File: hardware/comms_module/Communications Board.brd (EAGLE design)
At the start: 30 x 25 mm, 44 parts, among them U2 STC3115, X2 USB-MICROB

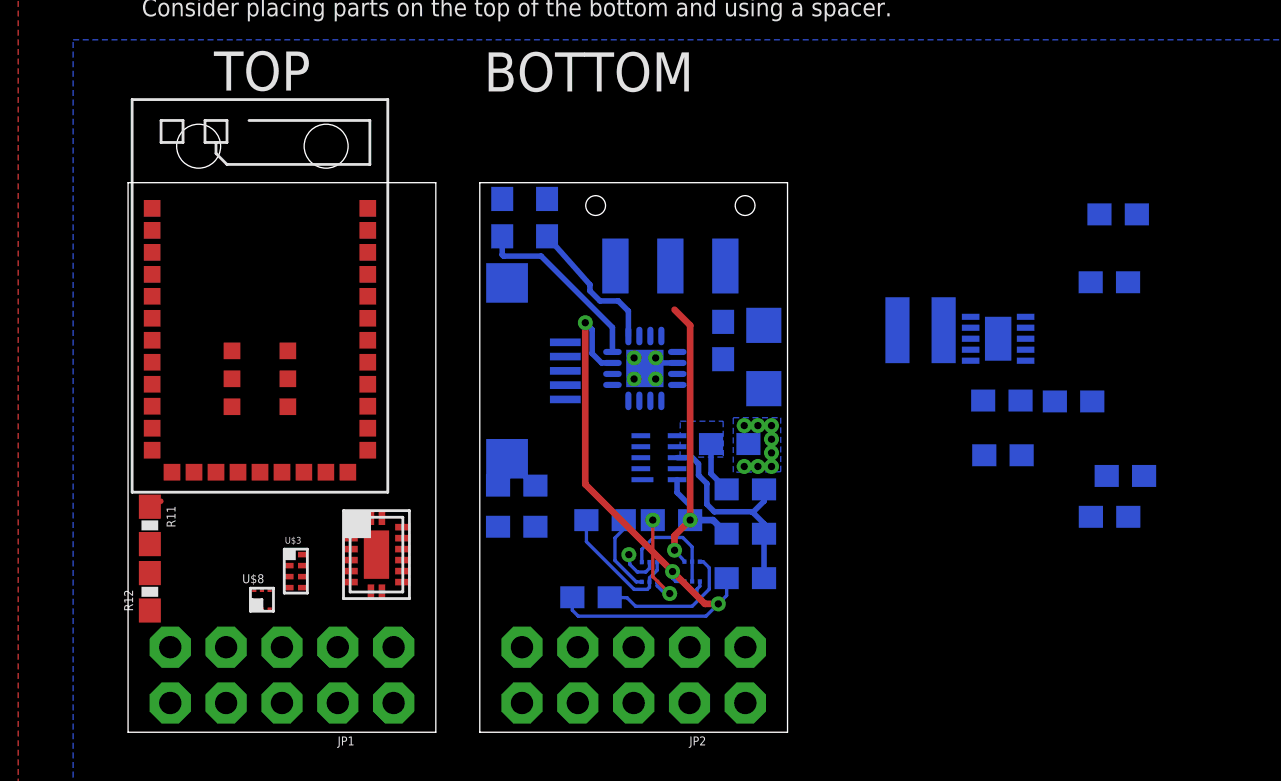
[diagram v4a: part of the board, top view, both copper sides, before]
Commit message: Continued routing of the communications board.
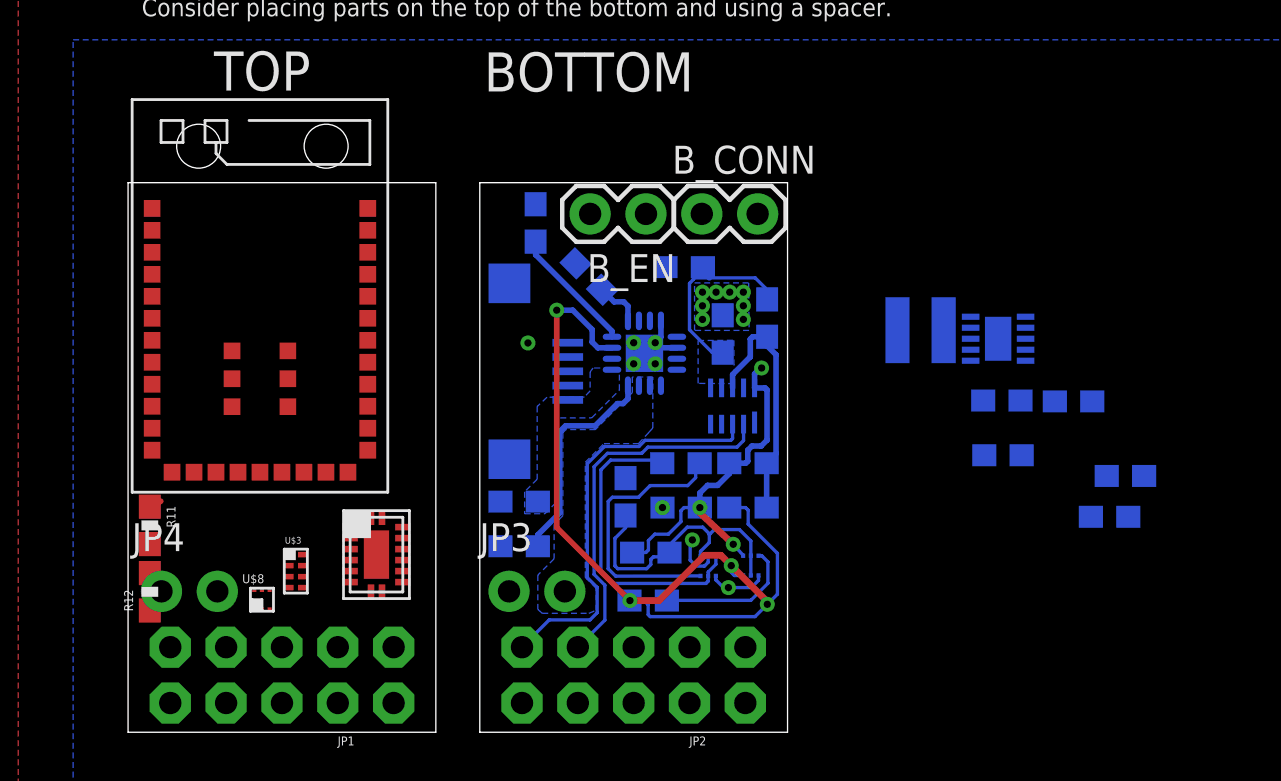
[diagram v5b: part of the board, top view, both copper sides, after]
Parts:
- removed PSW: (no value), Capstone Library:JS102011SAQN
- removed TP1, TP2: PTR1TP16SQ, testpad:TP16SQ
- added B_CONN, B_EN: (no value), SparkFun-Connectors:1X02
- added JP3, JP4: (no value), SparkFun-Connectors:1X02_NO_SILK
- moved R19 25.8 mm to (22.6, 10.7), turned to 270 degrees
- moved R18 24.2 mm to (23.8, 8.17), turned to 180 degrees
- moved R4 7.85 mm to (29.1, 18.8), turned to 270 degrees
- moved R5 5.02 mm to (27.1, 18.1), turned to 90 degrees
- moved R13 4.31 mm to (25.1, 12.2)
- moved U2 4.09 mm to (27.5, 14.8), turned to 0 degrees
- moved C5 3.78 mm to (25.3, 21.2), turned to 180 degrees
- moved R8 3.29 mm to (21.0, 20.7), turned to 225 degrees
- moved R17 3.21 mm to (28.2, 12.2)
- moved R6 3.21 mm to (28.2, 10.2)
- moved U$6 2.68 mm to (26.4, 7.56)
- moved U$7 2.68 mm to (28.3, 7.58)
- moved R16 2.60 mm to (23.7, 5.99)
- moved R7 1.54 mm to (18.5, 23.2)
- moved R2 0.90 mm to (17.8, 8.46)
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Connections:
- removed net N$6: PSW.3, TP2.TP
- new net B+IN: B_CONN.1, B_EN.1
- net +3V3: now also JP3.1, JP4.1
- net BAT+: now also B_EN.2; no longer PSW.2
- net BAT-: now also B_CONN.2; no longer TP1.TP
- net V_PREBUCK: now also JP3.2, JP4.2
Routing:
- net SCL: track 0.56 -> 19.3 mm
- net SDA: track 0.00 -> 17.0 mm
- net SYSOFF: track 28.1 -> 40.2 mm, vias 3 -> 4
- net N$23: track 0.00 -> 9.95 mm
- net N$12: track 3.63 -> 12.6 mm
- net N$22: track 4.84 -> 13.4 mm
- net N$9: track 6.08 -> 14.4 mm
- net BAT-: track 2.35 -> 8.97 mm
- net N$20: track 6.49 -> 2.16 mm
- net N$24: track 8.34 -> 5.77 mm
- net BATDC: track 9.79 -> 11.5 mm
- net GND: track 6.38 -> 5.49 mm, vias 14 -> 15
- net BAT+: track 16.2 -> 16.7 mm, vias 2 -> 3
- added copper zone on layer 16, net JACK_PWR
- added copper zone on layer 16, net V_PREBUCK

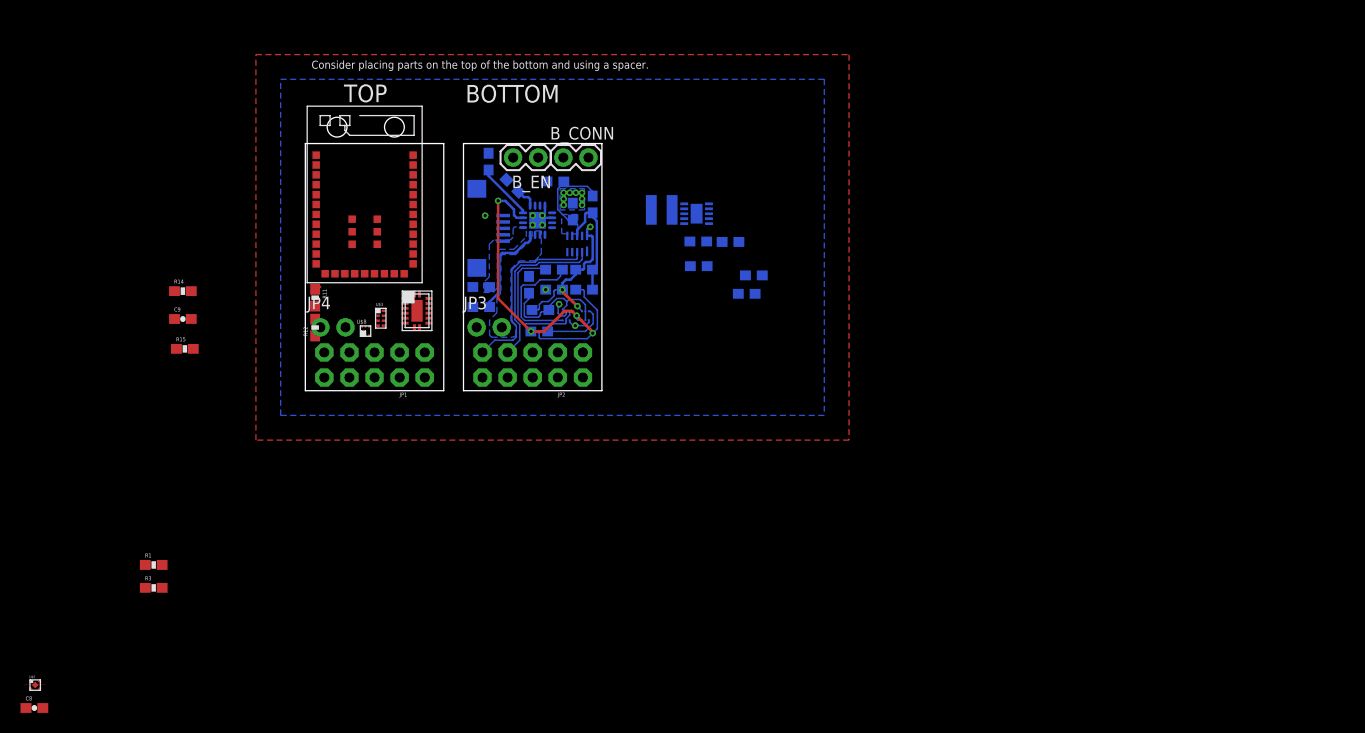
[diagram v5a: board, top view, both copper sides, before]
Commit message: Continued routing of top and bottom.
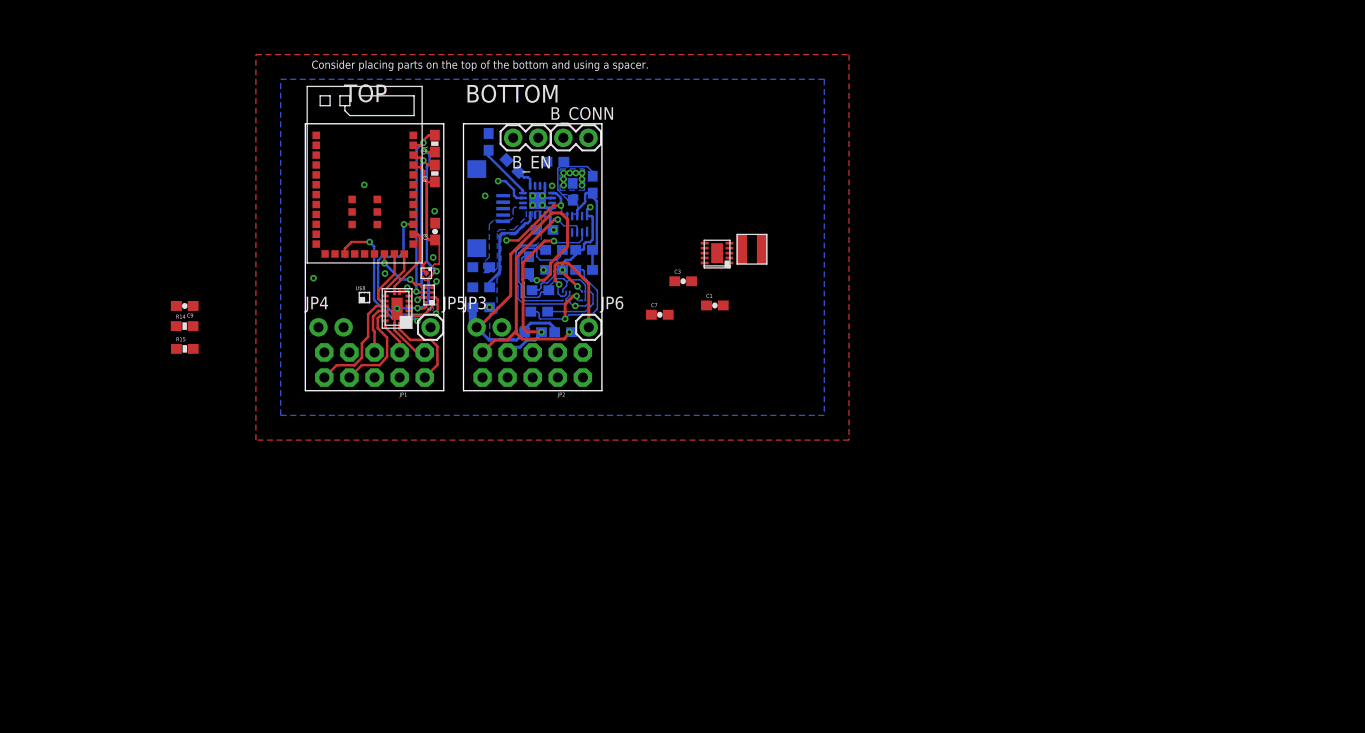
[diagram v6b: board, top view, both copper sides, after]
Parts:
- added JP5, JP6: (no value), SparkFun-Connectors:1X01
- moved C8 63.0 mm to (13.1, 16.1), turned to 90 degrees
- moved U$5 57.5 mm to (12.2, 11.9), turned to 270 degrees
- moved R1 51.2 mm to (13.1, 25.0), turned to 90 degrees
- moved R3 50.7 mm to (13.1, 22.0), turned to 90 degrees
- moved C10 26.9 mm to (17.8, 8.43), turned to 180 degrees
- moved R11 25.3 mm to (26.1, 5.93), flipped to the bottom, turned to 0 degrees
- moved R12 22.1 mm to (23.0, 5.93), flipped to the bottom, turned to 0 degrees
- moved C4 15.6 mm to (24.2, 16.3), turned to 180 degrees
- moved C7 10.3 mm to (35.9, 7.68), flipped to the top
- moved L1 9.96 mm to (45.2, 14.3), flipped to the top
- moved C3 6.23 mm to (38.2, 11.1), flipped to the top
- moved U$3 5.43 mm to (12.5, 9.68), turned to 90 degrees
- moved U$4 4.49 mm to (41.6, 13.9), flipped to the top
- moved C1 4.30 mm to (41.4, 8.62), flipped to the top
- moved R14 3.54 mm to (-12.2, 6.53)
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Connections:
- removed net N$11: U$1.7
- removed net N$13: JP1.8
- removed net N$14: R14.1, R15.2, U$6.5
- removed net N$15: JP1.6
- removed net N$16: JP1.3
- removed net N$19: JP1.1
- removed net N$7: JP1.9
- removed net VCC: R11.2, R12.2
- new net SYSDPASS: JP5.1, JP6.1, R14.1, R15.2, U$6.5
- net +3V3: now also R11.2, R12.2
- net BANDAGE_A_0: now also JP1.6
- net BANDAGE_A_1: now also JP1.3
- net BANDAGE_A_2: now also JP1.8
- net BANDAGE_A_3: now also JP1.1
- net BANDAGE_A_4: now also JP1.9
- net GND: now also U$1.7
- net MSW_0: now also MCU.20; no longer MCU.23
- net MSW_2: now also MCU.23; no longer MCU.20
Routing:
- net +3V3: track 0.00 -> 38.1 mm, vias 0 -> 1
- net PERIPHERAL_VCC: track 0.00 -> 31.2 mm, vias 0 -> 4
- net SYSOFF: track 40.2 -> 20.6 mm, vias 4 -> 3
- net MP_EN_SW: track 0.00 -> 19.3 mm, vias 0 -> 2
- net VSENSE_0: track 0.00 -> 19.1 mm, vias 0 -> 2
- net CONN_STATE_RD: track 0.00 -> 19.1 mm, vias 0 -> 2
- net VSENSE_1: track 0.00 -> 18.3 mm, vias 0 -> 2
- net +1V3: track 0.00 -> 13.7 mm
- net SYSDPASS: track 0.00 -> 13.1 mm, vias 0 -> 1
- net BANDAGE_A_3: track 0.00 -> 11.4 mm
- net BANDAGE_A_1: track 0.00 -> 9.86 mm
- net V_PREBUCK: track 0.00 -> 9.07 mm, vias 0 -> 2
- net BANDAGE_A_4: track 0.00 -> 8.65 mm
- net SCL: track 19.3 -> 26.8 mm, vias 0 -> 2
- net MSW_2: track 0.00 -> 7.41 mm
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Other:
- board size 30 x 25 mm -> 30 x 27 mm

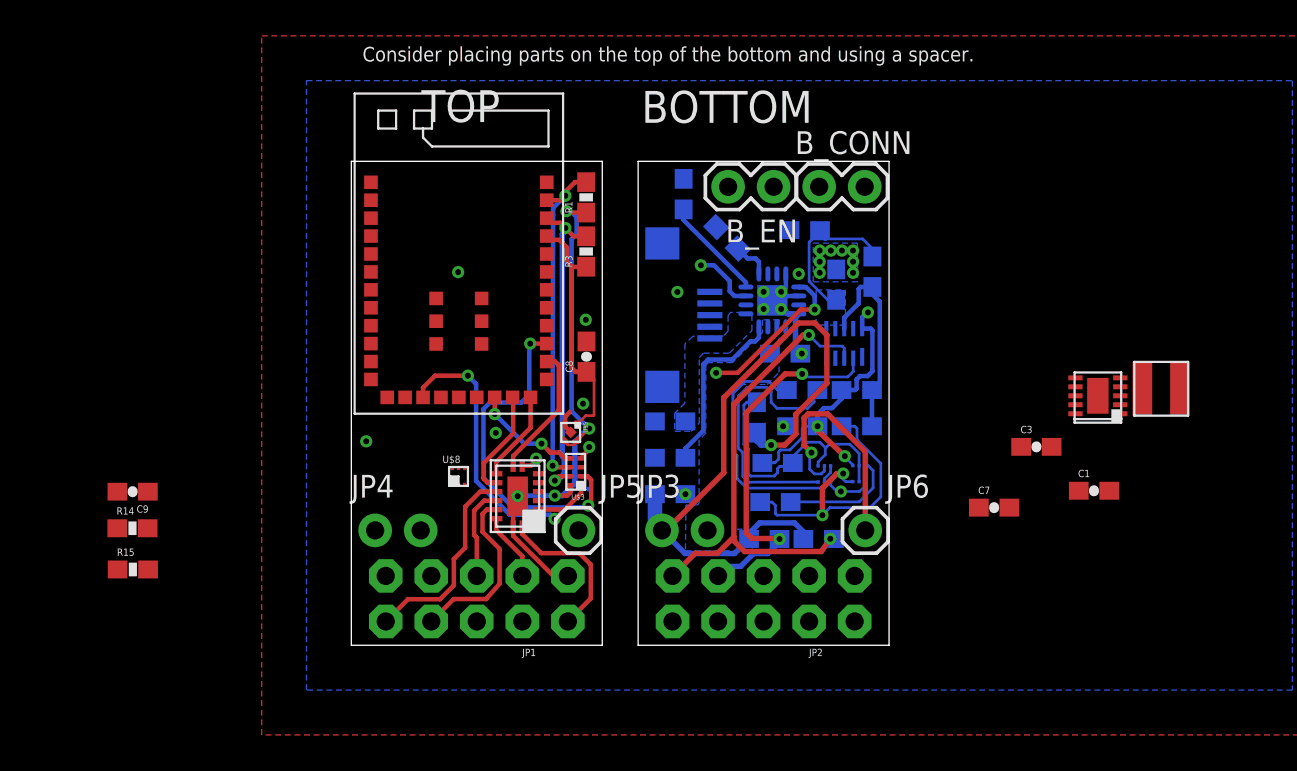
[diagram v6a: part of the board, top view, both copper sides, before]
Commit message: Convert to 4 layer. Nearly complete routing.
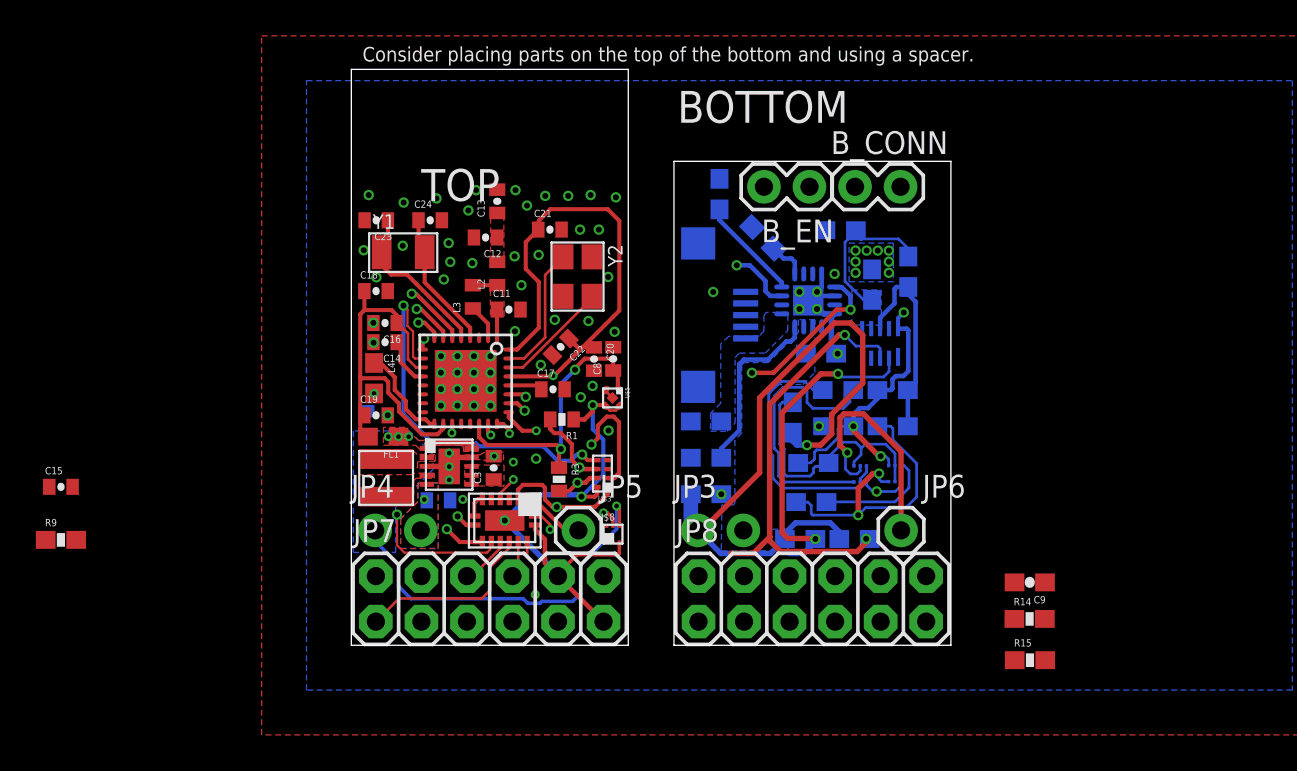
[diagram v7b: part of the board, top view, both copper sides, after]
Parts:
- removed JP1, JP2: (no value), SparkFun-Connectors:2X5_NOSILK
- removed MCU: SABLE-X-BLE-MODULE, Capstone Library:SABLE-X-BLE-MODULE
- added C11, C12: 1.2pF, SparkFun-Passives:0402-CAP
- added C13, C23, C24: 12pF, SparkFun-Passives:0402-CAP
- added C14: 1uF, SparkFun-Passives:0402-CAP
- added C15, C16, C17, C19, C21, C22: 100nF, SparkFun-Passives:0402-CAP
- added C18, C20: 10uF, SparkFun-Passives:0402-CAP
- added FL1: BLM18HE152SN1, Michael Blouin Library:0603
- added JP7, JP8: 2X6 FEMALE, SparkFun-Connectors:2X6
- added L2: 2nH, SparkFun-Passives:C0402
- added L3: 15nH, SparkFun-Passives:C0402
- added L4: 10uH, Michael Blouin Library:0603
- added R9: 100k, SparkFun-Passives:0603-RES
- added U1: Value, Capstone Library:RHB0032E
- added Y1: 32.768kHz, Capstone Library:CRYSTAL-3.2X1.5
- added Y2: 24MHz, Capstone Library:TSX-3225
- C1, C3, C7, C8: device SparkFun-Passives:0603-CAP -> SparkFun-Passives:0402-CAP
- R1, R3: device SparkFun-Passives:0603-RES -> SparkFun-Passives:0402-RES
- moved R14 50.3 mm to (37.8, 1.47)
- moved C9 50.3 mm to (37.9, 3.51)
- moved R15 50.3 mm to (37.9, -0.83)
- moved L1 43.5 mm to (1.94, 9.34), turned to 90 degrees
- moved C1 36.6 mm to (4.86, 8.09), flipped to the bottom, turned to 180 degrees
- moved U$4 36.4 mm to (5.46, 9.98), turned to 270 degrees
- moved C7 35.3 mm to (0.84, 12.4), flipped to the bottom, turned to 90 degrees
- moved C3 30.3 mm to (7.94, 9.90), turned to 90 degrees
- moved R3 12.8 mm to (11.6, 9.26), turned to 270 degrees
- moved R1 12.5 mm to (11.8, 12.6), turned to 180 degrees
- moved U$8 9.20 mm to (14.6, 6.20)
- moved U$5 3.02 mm to (14.6, 13.8)
- moved B_CONN 2.00 mm to (28.1, 25.6)
- moved B_EN 2.00 mm to (25.6, 25.6)
- moved C10 2.00 mm to (19.8, 8.43)
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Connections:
- removed net BANDAGE_DETECT: U$1.5
- removed net SYSDPASS: JP5.1, JP6.1, R14.1, R15.2, U$6.5
- new net ANTENNA: C13.2
- new net DCDC_SW: L4.1, U1.17
- new net N$18: C23.1, U1.5, Y1.1
- new net N$19: C24.1, U1.4, Y1.2
- new net N$41: C12.1, C13.1, L2.2
- new net N$43: C14.1, U1.12
- new net PERIPHERAL_DETECT: JP7.12, JP8.12, U$1.5
- new net RF_N: L3.1, U1.2
- new net RF_P: C11.1, L2.1, L3.2, U1.1
- new net VCC: C16.1, C17.1, C18.1, C19.1, FL1.2, R9.2, U1.11, U1.18, U1.28
- new net VDDR: C20.1, C21.1, C22.1, L4.2, U1.29, U1.32
- new net X24M_N: U1.30, Y2.3
- new net X24M_P: U1.31, Y2.1
- net +1V3: now also U1.22; no longer MCU.30
- net +3V3: now also FL1.1; no longer MCU.11, MCU.12
- net /SYSDISBL: now also JP5.1, JP6.1, R14.1, R15.2, U$6.5
- net AGND: now also JP8.5; no longer JP1.5, JP2.5
- net BANDAGE_A_0: now also JP7.6, U$1.12, U1.23; no longer JP1.6, MCU.29, U$1.13
- net BANDAGE_A_1: now also JP7.3, U$1.15; no longer JP1.3, U$1.14
- net BANDAGE_A_2: now also JP7.8, U$1.14; no longer JP1.8, U$1.15
- net BANDAGE_A_3: now also JP7.1, U$1.13; no longer JP1.1, U$1.12
- net BANDAGE_A_4: now also JP7.9; no longer JP1.9
- net CONN_STATE_RD: now also U1.25; no longer MCU.15
- net GND: now also C11.2, C12.2, C14.2, C15.2, C16.2, C17.2, C18.2, C19.2, C20.2, C21.2, C22.2, C23.2, C24.2, JP7.5, JP7.7, JP8.7, U1.33, Y2.2, Y2.4; no longer JP1.7, JP2.7, MCU.2, MCU.22, MCU.3, MCU.33, MCU.34, MCU.35, MCU.36, MCU.37, MCU.38, MCU.39
- net JTAG_TCKC: now also U1.14; no longer MCU.7
- net JTAG_TDI: now also U1.16; no longer MCU.14
- net JTAG_TDO: now also U1.15; no longer MCU.13
- net JTAG_TSMC: now also U1.13; no longer MCU.8
- net MCU_RST: now also C15.1, R9.1, U1.19; no longer MCU.6
- net MPSW: now also U1.10; no longer MCU.19
- net MP_EN_SW: now also U1.6; no longer MCU.24
- net MSW_0: now also U1.7; no longer MCU.20
- net MSW_1: now also U1.8; no longer MCU.21
- net MSW_2: now also U1.9; no longer MCU.23
- net N$25: now also JP8.9; no longer JP2.9
- net N$26: now also JP8.8; no longer JP2.8
- net N$27: now also JP8.6; no longer JP2.6
- net N$28: now also JP8.3; no longer JP2.3
- net N$29: now also JP8.1; no longer JP2.1
- net PERIPHERAL_PWR: now also U1.24; no longer MCU.18
- net PERIPHERAL_VCC: now also JP7.10, JP7.11, JP8.10, JP8.11; no longer JP1.10, JP2.10
- net SCL: now also JP7.2, JP8.2, U1.27; no longer JP1.2, JP2.2, MCU.17
- net SDA: now also JP7.4, JP8.4, U1.26; no longer JP1.4, JP2.4, MCU.16
- net VSENSE_0: now also U1.20; no longer MCU.32
- net VSENSE_1: now also U1.21; no longer MCU.31
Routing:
- net VDDR: track 0.00 -> 40.8 mm, vias 0 -> 2
- net +3V3: track 38.1 -> 61.7 mm, vias 1 -> 5
- net VCC: track 0.00 -> 23.2 mm
- net MSW_0: track 6.01 -> 23.6 mm, vias 0 -> 2
- net /SYSDISBL: track 0.00 -> 16.7 mm, vias 0 -> 1
- net VSENSE_1: track 18.3 -> 2.43 mm, vias 2 -> 1
- net MPSW: track 6.30 -> 21.8 mm
- net SCL: track 26.8 -> 41.8 mm, vias 2 -> 3
- net VSENSE_0: track 19.1 -> 4.60 mm, vias 2 -> 1
- net SYSDPASS: track 13.1 -> 0.00 mm, vias 1 -> 0
- net MSW_1: track 5.06 -> 16.9 mm, vias 0 -> 2
- net SDA: track 20.9 -> 31.5 mm, vias 2 -> 3
- net PERIPHERAL_PWR: track 0.00 -> 9.83 mm, vias 0 -> 2
- net PERIPHERAL_DETECT: track 0.00 -> 9.64 mm, vias 0 -> 1
- net N$18: track 0.00 -> 9.08 mm
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- added copper zone on layer 1, net +3V3
- added copper zone on layer 16, net +3V3
- added copper zone on layer 15, net GND
- added copper zone on layer 2, net GND
- added copper zone on layer 1, net N$10
- added copper zone on layer 1, net N$41
- added copper zone on layer 1, net N$5
- added copper zone on layer 1, net N$8
- added copper zone on layer 1, net RF_P
- added copper zone on layer 1, net V_PREBUCK
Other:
- board size 30 x 27 mm -> 33.5 x 32.1 mm
